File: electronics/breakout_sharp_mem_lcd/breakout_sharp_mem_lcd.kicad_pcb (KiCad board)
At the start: 2 copper layers, 2 parts

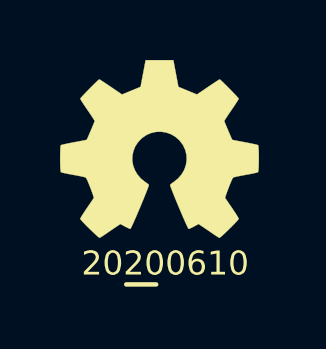
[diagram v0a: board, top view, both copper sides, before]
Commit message: updated board with versionnumber
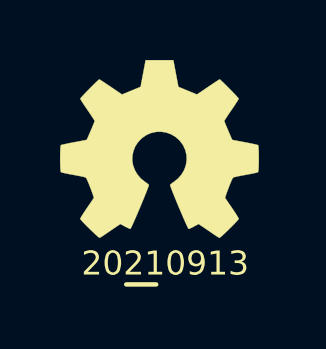
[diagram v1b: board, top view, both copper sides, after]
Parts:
- N1: value 20200610 -> 20210913
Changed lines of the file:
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@@
-(kicad_pcb (version 20171130) (host pcbnew 5.1.6-c6e7f7d~86~ubuntu19.10.1)
+(kicad_pcb (version 20171130) (host pcbnew 5.1.10-88a1d61d58~90~ubuntu21.04.1)
   (general
     (thickness 1.6)
@@
       (effects (font (size 1 1) (thickness 0.15)))
     )
-    (fp_text value 20200610 (at 0.8 -0.1) (layer F.SilkS)
+    (fp_text value 20210913 (at 0.8 -0.1) (layer F.SilkS)
       (effects (font (size 0.8 0.8) (thickness 0.15)))
     )

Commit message: started with inital layout
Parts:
- added C1: 1u, SquantorRcl:C_0402, F.Cu at (154.0, 69.7)
- added C2: 1u, SquantorRcl:C_0402, F.Cu at (157.6, 63.9)
- added C3: 1n, SquantorRcl:C_0402, F.Cu at (154.0, 70.8)
- added FB1: 600, SquantorRcl:L_0402, F.Cu at (155.9, 64.4)
- added FB2: 600, SquantorRcl:L_0402, F.Cu at (155.9, 63.3)
- added J1: Conn_01x06, Connector_JST:JST_PH_B6B-PH-SM4-TB_1x06-1MP_P2.00mm_Vertical, F.Cu at (142.0, 71.0)
- added J2: Conn_01x10, Connector_FFC-FPC:TE_1-1734839-0_1x10-1MP_P0.5mm_Horizontal, F.Cu at (158.0, 71.0)
- added JP1: EXTMODE, SquantorSpecial:solder_jumper_3way_12conn, F.Cu at (152.9, 67.1)
- added JP2: 5V, SquantorSpecial:solder_jumper_2way_noconn, F.Cu at (148.8, 76.4)
- added R1: 10K, SquantorRcl:R_0402_hand, F.Cu at (154.0, 71.9)
- N1, N2: moved to B.Cu
- moved N1 22.0 mm to (151.3, 73.9), turned to 180 degrees
- moved N2 21.3 mm to (150.7, 70.0), turned to 180 degrees
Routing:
- net /VDD: track 0.00 -> 29.3 mm, vias 0 -> 3
- net /EXTCOMIN: track 0.00 -> 19.0 mm
- net /SCS: track 0.00 -> 16.9 mm
- net /VDDA: track 0.00 -> 16.7 mm
- net /SI: track 0.00 -> 16.1 mm
- net /SCLK: track 0.00 -> 15.5 mm
- net /VSSA: track 0.00 -> 12.5 mm
- net /VSS: track 0.00 -> 11.3 mm, vias 0 -> 4
- net /VDD_IN: track 0.00 -> 6.65 mm
- net /EXTMODE: track 0.00 -> 5.49 mm
- net /DISP: track 0.00 -> 2.29 mm
- added copper zone on B.Cu, net /VSS
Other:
- board outline added: 26 x 18 mm

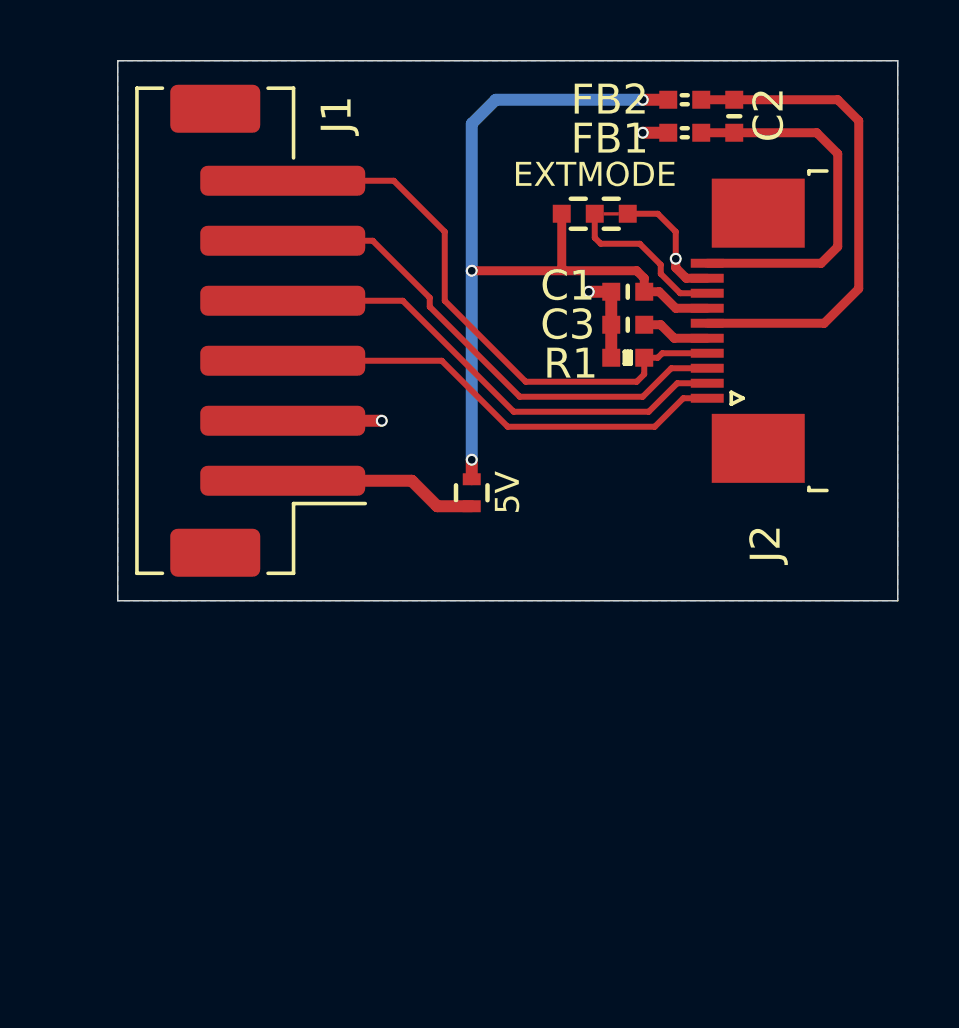
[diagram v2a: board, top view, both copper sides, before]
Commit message: added extra ground plane to PCB, added REG710 step up converter
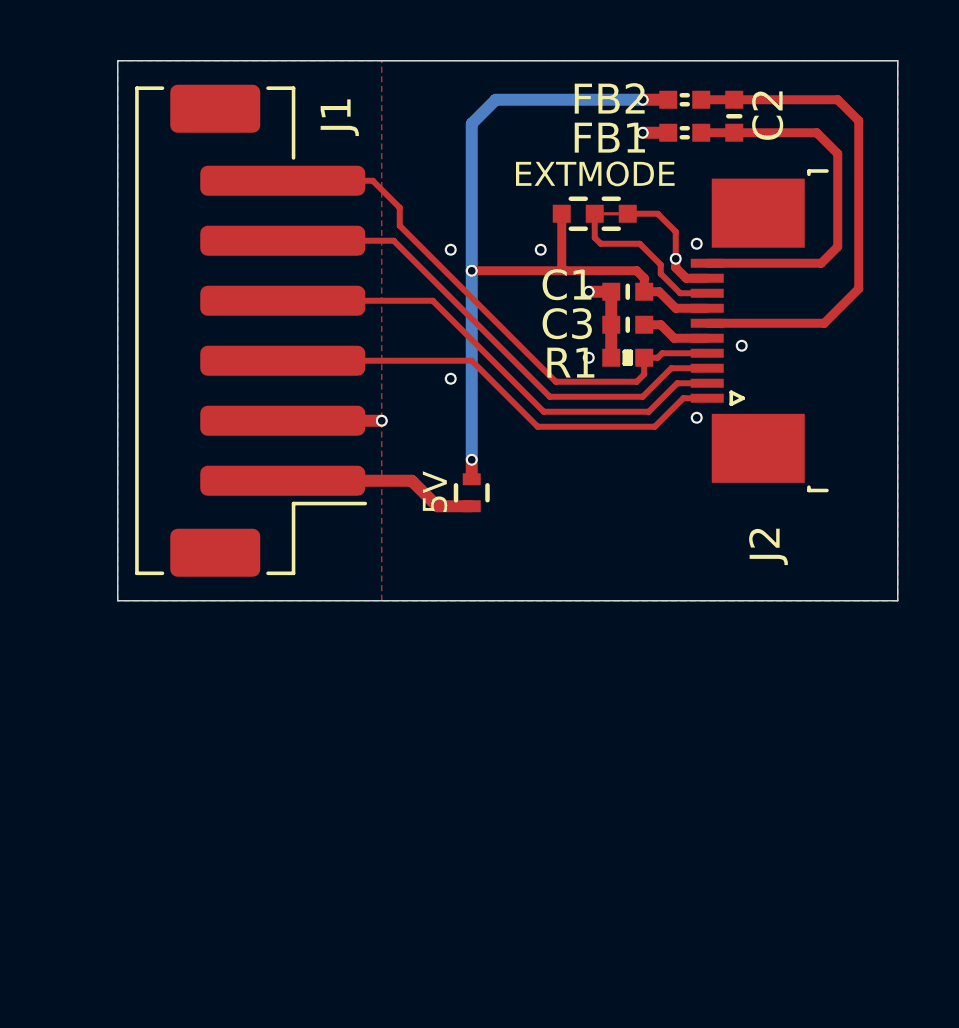
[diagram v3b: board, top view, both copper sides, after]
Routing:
- net /EXTCOMIN: track 19.0 -> 18.0 mm
- net /VSS: vias 4 -> 11
- added copper zone on F.Cu, net /VSS

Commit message: placed, routed, silk placed, optimized
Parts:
- added C4: 2.2u, SquantorRcl:C_0603, F.Cu at (146.5, 76.7)
- added C5: 2.2u, SquantorRcl:C_0603, F.Cu at (151.4, 78.5)
- added C6: 0.22u, SquantorRcl:C_0603, F.Cu at (147.9, 76.0)
- added R2: 10K, SquantorRcl:R_0402_hand, F.Cu at (153.4, 75.3)
- added U1: REG710, SquantorIC:SOT23-6-HAND, F.Cu at (150.7, 76.0)
- N1: value 20210913 -> 20210927
- moved JP2 3.11 mm to (146.5, 74.3)
- moved C2 1.60 mm to (155.9, 63.9)
- moved C1 1.60 mm to (152.4, 69.7)
- moved C3 1.60 mm to (152.4, 70.8)
- moved FB1 1.60 mm to (154.3, 64.4)
- moved FB2 1.60 mm to (154.3, 63.3)
- moved J2 1.60 mm to (156.4, 71.0)
- moved JP1 1.60 mm to (151.3, 67.1)
- moved R1 1.60 mm to (152.4, 71.9)
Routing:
- net /VDD_IN: track 6.65 -> 21.9 mm, vias 0 -> 2
- net /VDD: track 29.3 -> 38.4 mm, vias 3 -> 4
- net /SCS: track 16.7 -> 15.0 mm
- net /SCLK: track 15.5 -> 13.8 mm
- net /SI: track 16.1 -> 14.4 mm
- net Net-(C6-Pad2): track 0.00 -> 1.68 mm
- net Net-(C6-Pad1): track 0.00 -> 1.68 mm
- net Net-(R2-Pad1): track 0.00 -> 1.62 mm
- net /EXTCOMIN: track 18.0 -> 16.7 mm
- net /VDDA: track 16.7 -> 16.0 mm
- net /VSS: track 11.3 -> 11.0 mm, vias 11 -> 14
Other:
- board size 26 x 18 mm -> 23.7 x 18 mm

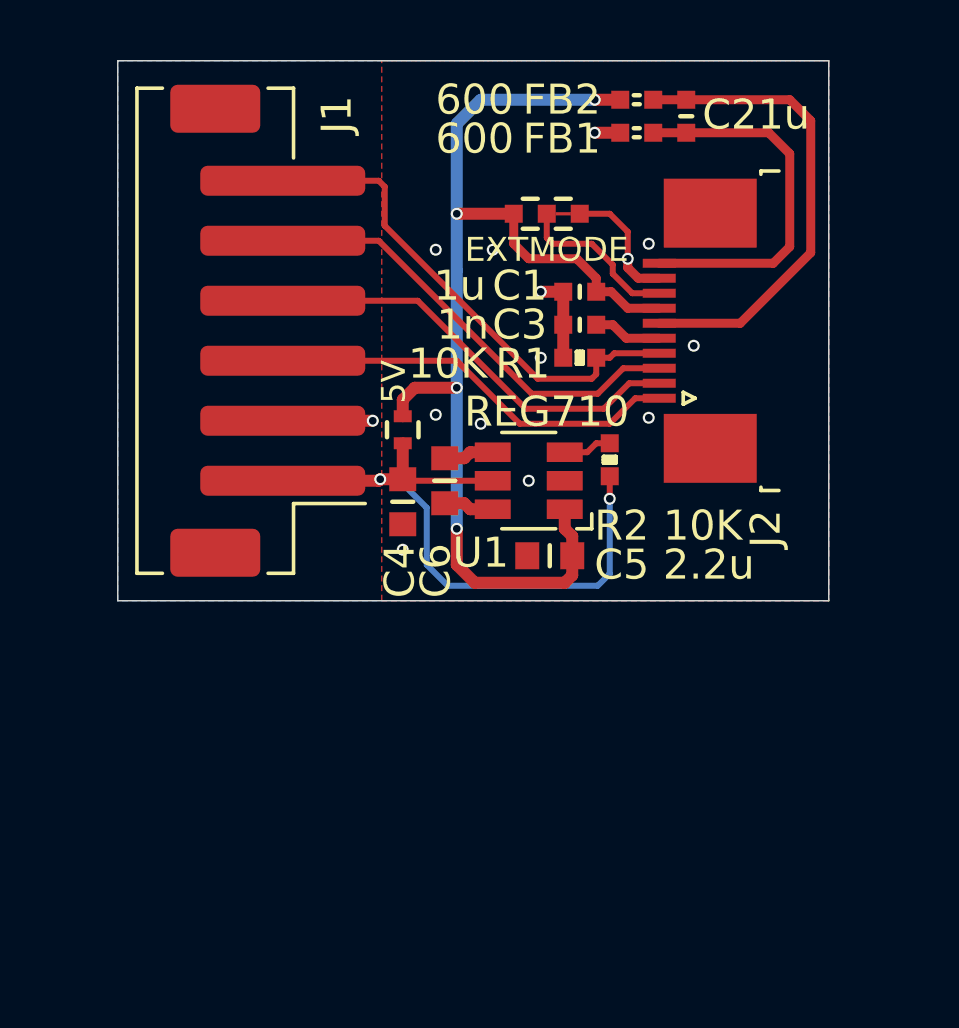
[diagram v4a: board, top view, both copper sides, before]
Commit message: fixed mistake, missing resistor on DISP
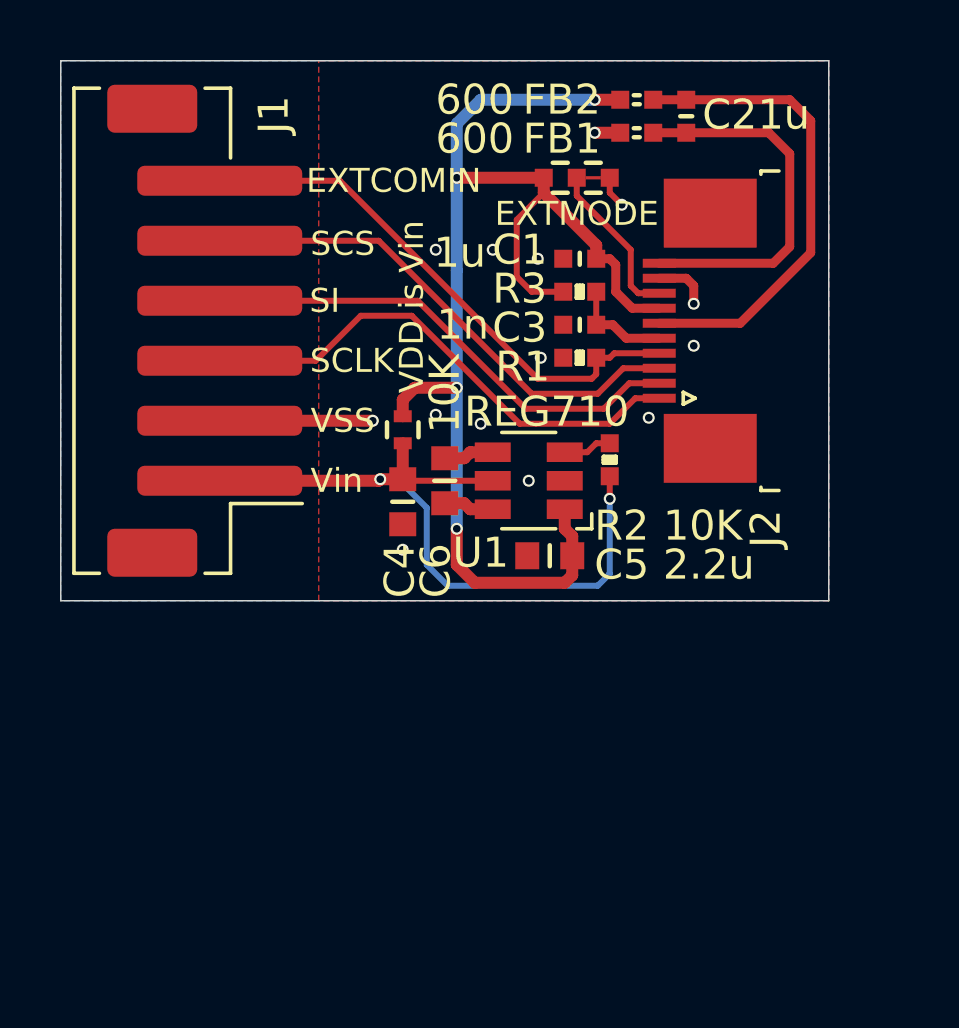
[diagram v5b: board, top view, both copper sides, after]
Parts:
- added R3: 10K, SquantorRcl:R_0402_hand, F.Cu at (152.4, 69.7)
- JP2: value 5V -> VDD is Vin
- N1: value 20210927 -> 20210930
- moved J1 2.10 mm to (139.9, 71.0)
- moved JP1 1.56 mm to (152.3, 65.9)
- moved C1 1.10 mm to (152.4, 68.6)
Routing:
- net /VDD: track 38.4 -> 44.1 mm
- net /VSS: track 11.0 -> 6.77 mm
- net /SCLK: track 13.8 -> 17.1 mm
- net /DISP: track 2.29 -> 3.39 mm
- net /EXTCOMIN: track 16.7 -> 16.0 mm
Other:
- board size 23.7 x 18 mm -> 25.6 x 18 mm
- board text added: "EXTCOMIN"
- board text added: "SCLK"
- board text added: "SCS"
- board text added: "SI"
- board text added: "VSS"
- board text added: "Vin"

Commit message: final checks before production
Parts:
- JP2: value VDD is Vin -> 5V
- N1: value 20210930 -> 20211001
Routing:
- net /VDD_IN: track 21.9 -> 22.5 mm

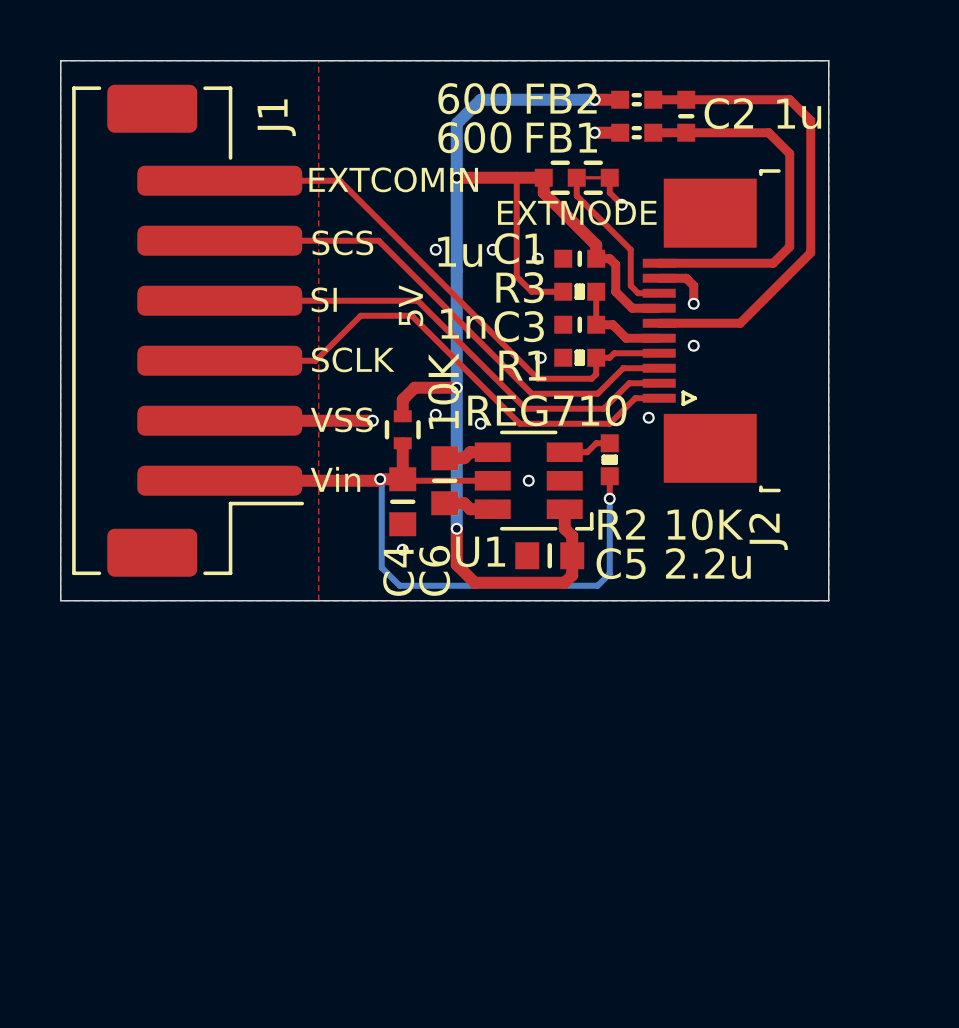
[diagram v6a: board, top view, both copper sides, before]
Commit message: minor silk changes
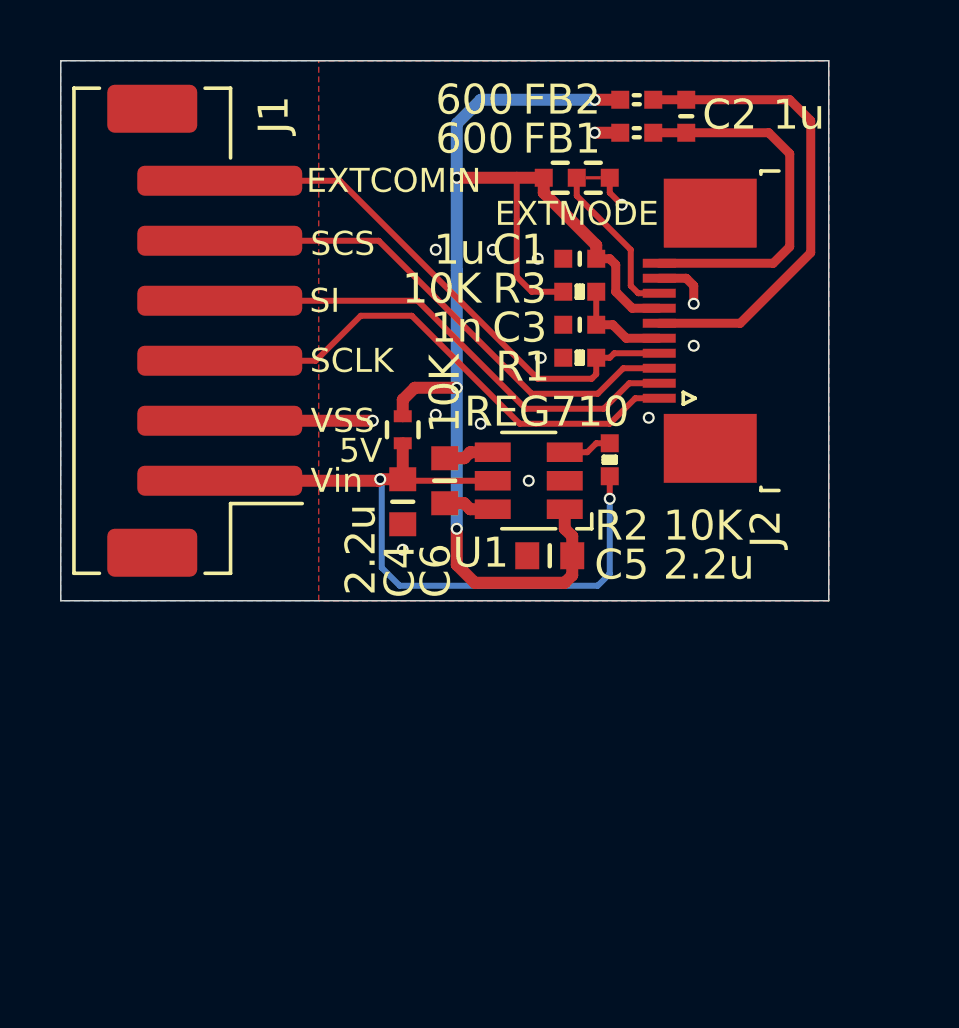
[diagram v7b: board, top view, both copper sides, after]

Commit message: updated versionnumber
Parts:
- N1: value 20211001 -> 20211012
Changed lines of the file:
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@@
       (effects (font (size 1 1) (thickness 0.15)) (justify mirror))
     )
-    (fp_text value 20211001 (at 0.8 0.1) (layer B.SilkS)
+    (fp_text value 20211012 (at 0.8 0.1) (layer B.SilkS)
       (effects (font (size 0.8 0.8) (thickness 0.15)) (justify mirror))
     )
